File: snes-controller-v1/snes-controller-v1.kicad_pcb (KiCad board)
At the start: 2 copper layers, 66.1 x 20.1 mm, 19 parts, among them J1 USB_B_Micro, J2 NES, J3 Conn_01x06, U1 SN74LVC125ADR, U2 AP2112K-3.3, U7 ATSAMD21E18A-A

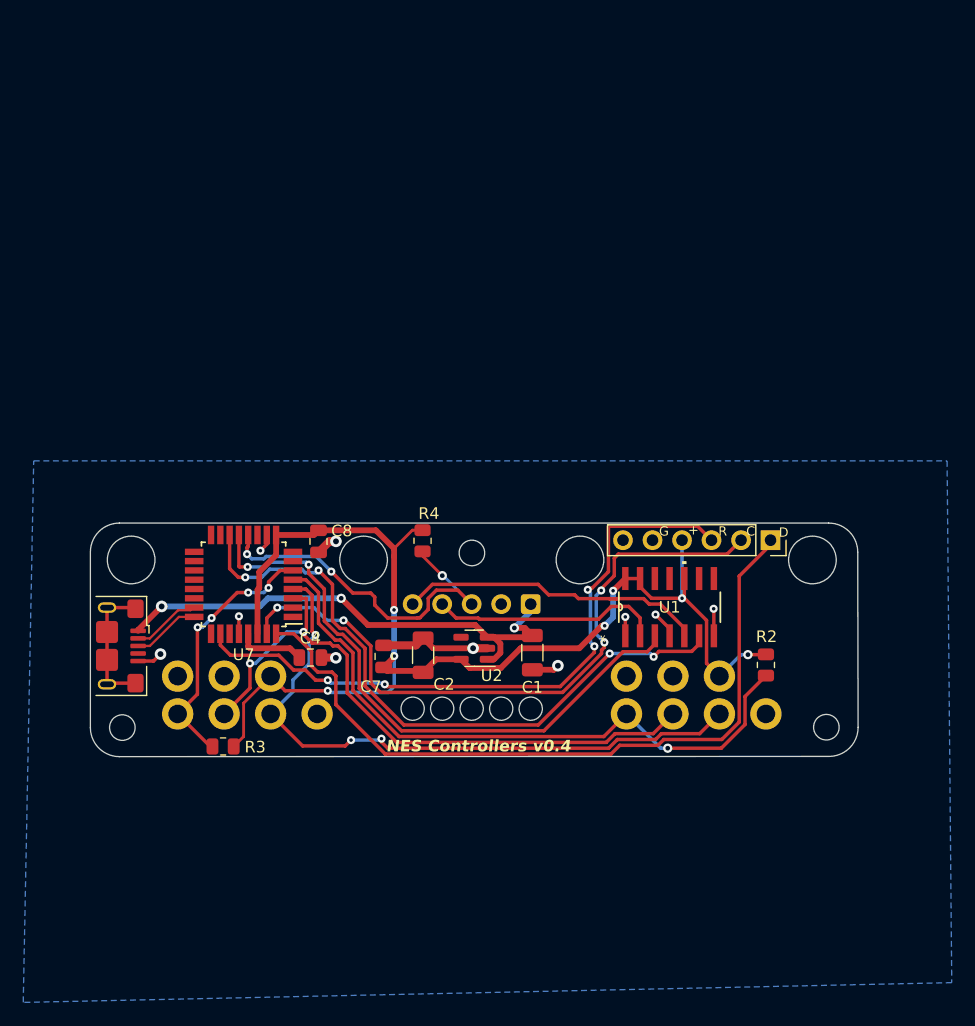
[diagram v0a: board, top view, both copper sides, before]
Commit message: update socket on PCB
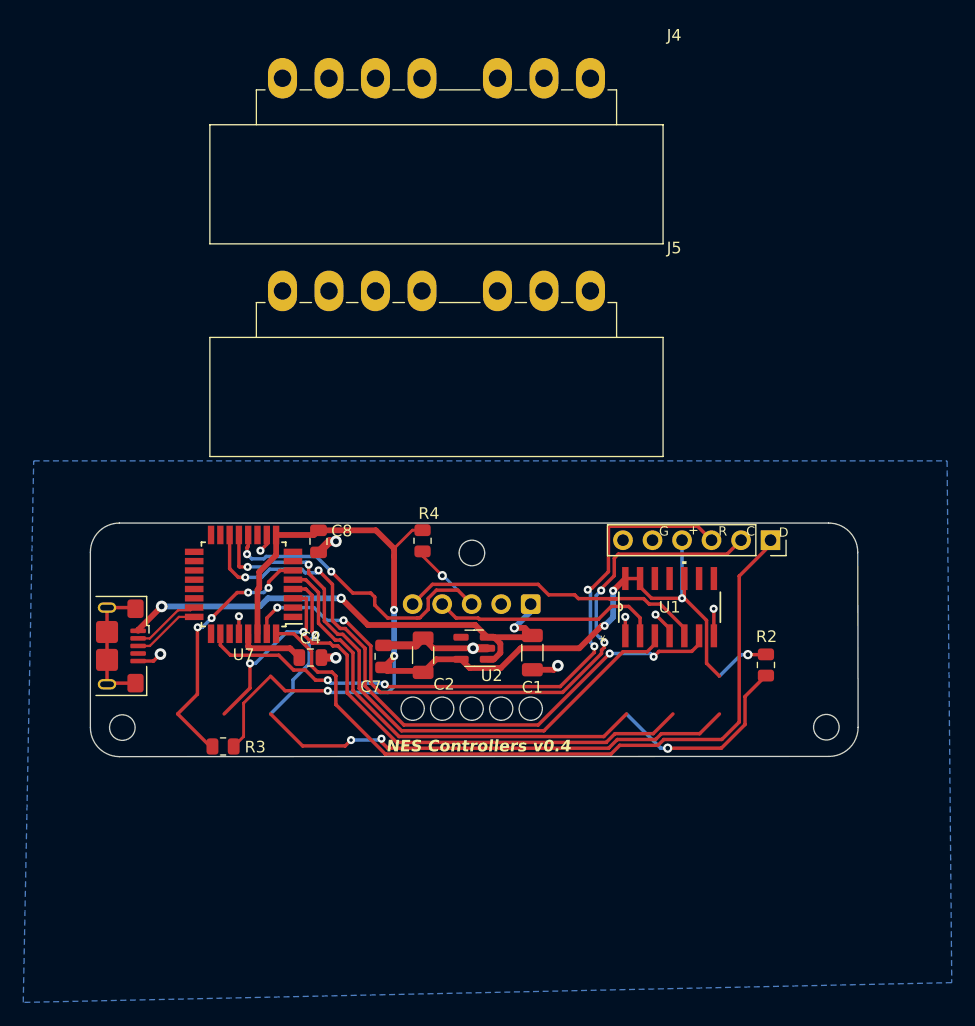
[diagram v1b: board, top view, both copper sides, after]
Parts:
- removed U3, U4: ~, Minor_Industries:NES controller port
- added J4: SNES_Controller_Socket, Minor_Industries:SNES_Controller_Socket, F.Cu at (124.1, 26.0)
- added J5: SNES_Controller_Socket, Minor_Industries:SNES_Controller_Socket, F.Cu at (124.1, 44.3)

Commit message: ground plane
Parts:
- removed C8: 1uF, Capacitor_SMD:C_0805_2012Metric
- J3: value Conn_01x06 -> Conn_01x05; footprint Connector_PinSocket_2.54mm:PinSocket_1x06_P2.54mm_Vertical -> Connector_PinSocket_2.54mm:PinSocket_1x05_P2.54mm_Vertical
- moved J1 63.2 mm to (172.2, 74.4), turned to 90 degrees
- moved J4 61.9 mm to (170.9, 66.5), turned to 180 degrees
- moved J5 42.9 mm to (144.8, 81.9)
- moved R3 41.1 mm to (160.1, 81.9), turned to 90 degrees
- moved J3 36.0 mm to (134.1, 82.3)
- moved H1 32.6 mm to (139.2, 66.8)
- moved U7 31.7 mm to (152.1, 74.2), turned to 0 degrees
- moved C2 29.5 mm to (165.6, 78.2), turned to 0 degrees
- moved U2 20.1 mm to (160.6, 76.9), turned to 0 degrees
- moved C4 19.0 mm to (144.9, 70.9), turned to -90 degrees
- moved U1 18.9 mm to (138.7, 74.2), turned to 0 degrees
- moved H3 15.0 mm to (139.2, 81.8)
- moved C1 14.6 mm to (159.8, 71.8), turned to 90 degrees
- moved J2 14.6 mm to (133.2, 79.0), turned to 90 degrees
- moved C7 11.7 mm to (144.5, 76.2)
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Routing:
- net /NES_CLOCK_3V: track 57.2 -> 20.0 mm, vias 4 -> 2
- net /PAD_DATA_1: track 55.8 -> 21.2 mm, vias 1 -> 2
- net /NES_LATCH_3V: track 52.4 -> 20.2 mm
- net /SWDIO: track 64.2 -> 34.8 mm
- net /PAD_CLOCK: track 55.5 -> 32.3 mm
- net /SWCLK: track 57.6 -> 36.6 mm, vias 4 -> 2
- net /PAD_LATCH: track 53.9 -> 35.2 mm, vias 2 -> 4
- net /NES_LATCH_5V: track 20.7 -> 3.18 mm
- net /NES_CLOCK_5V: track 26.3 -> 11.1 mm
- net /RESET: track 57.2 -> 45.3 mm, vias 4 -> 0
- net /D-: track 5.82 -> 14.5 mm
- net /D+: track 5.76 -> 14.4 mm
- net GND: track 26.7 -> 19.1 mm, vias 10 -> 9
- net +3V3: track 107.3 -> 113.1 mm, vias 7 -> 2
- net /PAD_DATA_2: track 22.8 -> 18.3 mm, vias 4 -> 1
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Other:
- board size 66.1 x 20.1 mm -> 51 x 20.1 mm
- board text added: "SNES v0.1"
- board text removed: "NES Controllers v0.4"
